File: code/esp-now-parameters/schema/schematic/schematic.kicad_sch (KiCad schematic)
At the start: 14 parts

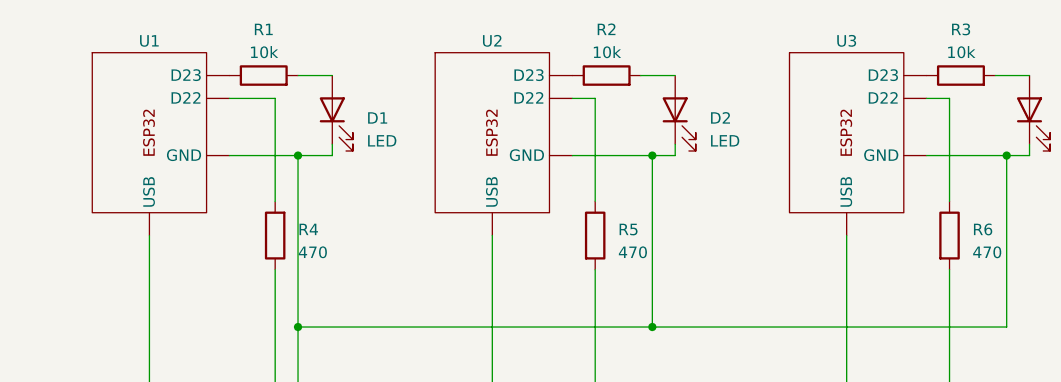
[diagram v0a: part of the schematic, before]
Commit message: Update pin22 to 21
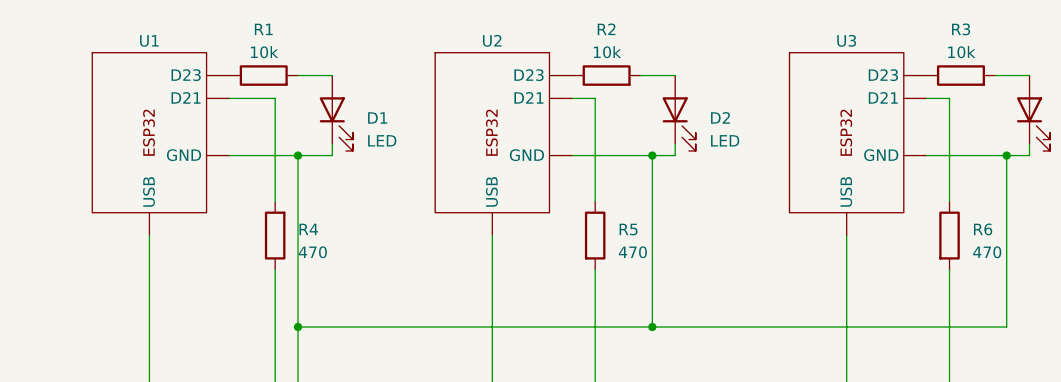
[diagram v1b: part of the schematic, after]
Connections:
- net at STM1. (USB): now also R4.1, R5.2, R6.2; no longer USBHUB1. (USB_PC)
- net at U2. (USB): now also R5.1; no longer USBHUB1. (USB_PC)
- net at U3. (USB): now also R6.1; no longer USBHUB1. (USB_PC)
- net at U1. (USB): now also R1.1; no longer USBHUB1. (USB_PC)
- new net: STM1. (USB), USBHUB1. (USB_PC)
- new net: U2. (USB), USBHUB1. (USB_PC)
- new net: U3. (USB), USBHUB1. (USB_PC)
- new net: U1. (USB), USBHUB1. (USB_PC)
- new net: D1.1 (K), D2.1 (K), D3.1 (K), STM1. (USB), U1. (USB), U2. (USB), U3. (USB)
